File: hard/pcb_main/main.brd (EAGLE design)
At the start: 230 x 150 mm, 865 parts

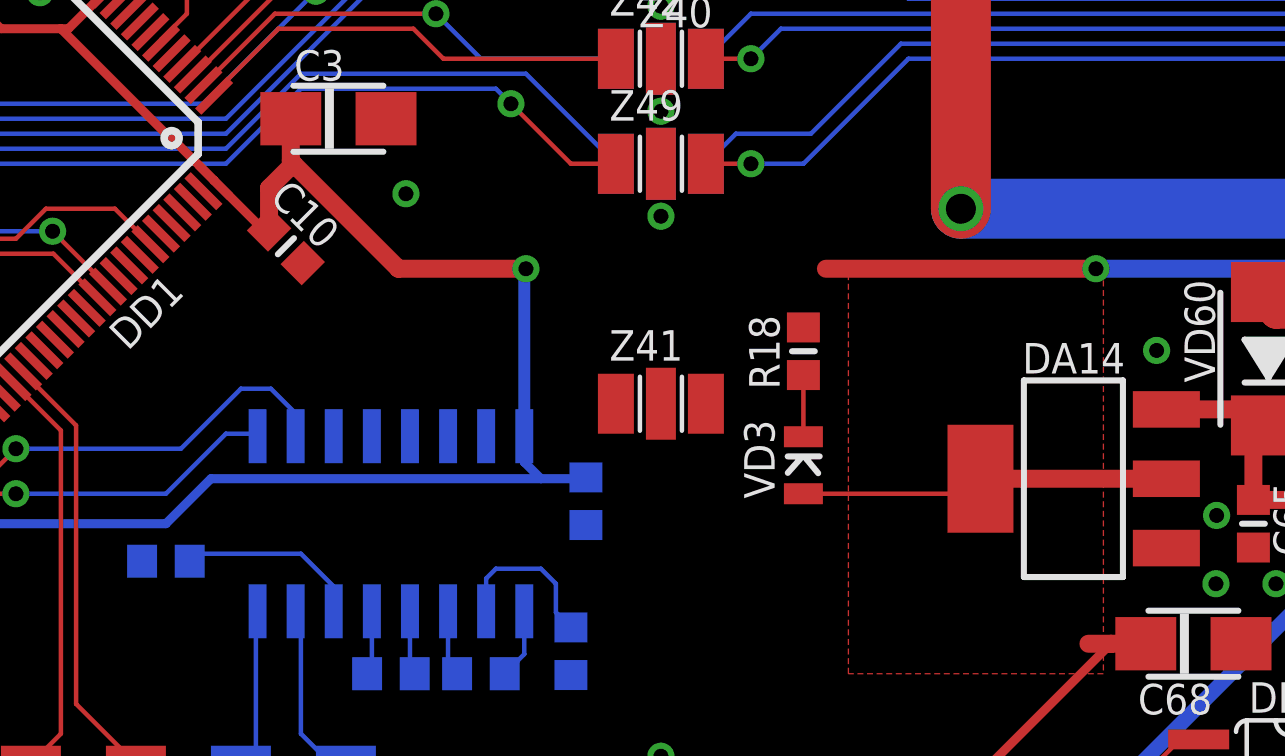
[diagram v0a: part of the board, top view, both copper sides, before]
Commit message: filters addition completed
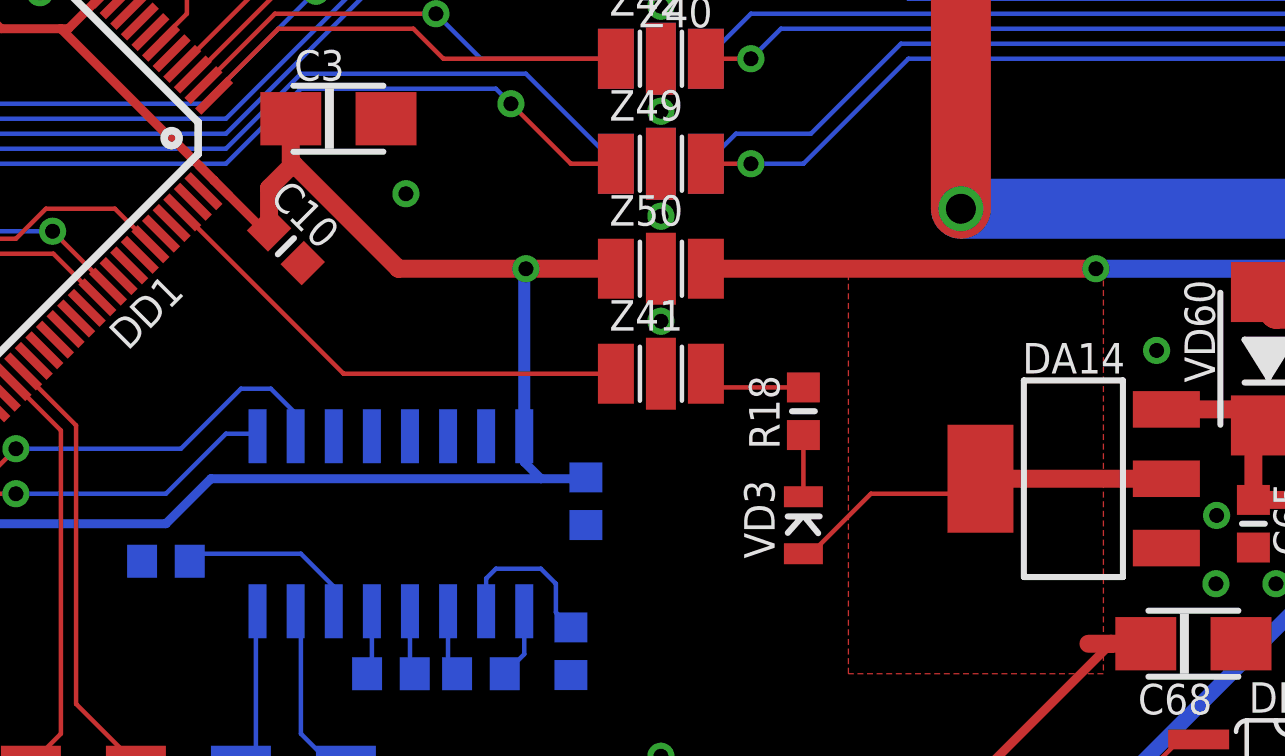
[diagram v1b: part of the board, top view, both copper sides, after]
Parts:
- added Z50: NFE31PT, emi-filter:NFE31
- moved R18 2.00 mm to (72.2, 65.8)
- moved VD3 2.00 mm to (72.2, 62.0)
- moved Z41 1.00 mm to (67.5, 67.0)
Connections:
- new net +3V3_DIRT: C1.1, C10.1, C143.1, C2.1, C3.+, C7.1, C9.1, DA17.16, DD1.100, DD1.11, DD1.28, DD1.50, DD1.6, DD1.75, L1.1, Z50.1
- net +3V3: now also Z50.3; no longer C1.1, C10.1, C143.1, C2.1, C3.+, C7.1, C9.1, DA17.16, DD1.100, DD1.11, DD1.28, DD1.50, DD1.6, DD1.75, L1.1
- net GND: now also Z50.2
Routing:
- net +3V3_DIRT: track 0.00 -> 99.6 mm, vias 0 -> 3
- net +3V3: track 902.7 -> 810.8 mm, vias 20 -> 17
- net N$350: track 0.00 -> 16.7 mm
- net N$272: track 0.00 -> 3.44 mm
- net GND: vias 169 -> 170

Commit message: nop
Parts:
- moved C3 2.12 mm to (55.2, 74.0), turned to 315 degrees
- moved VD1 0.52 mm to (7.88, 100.8)
- moved Z10 0.50 mm to (15.0, 74.0)
- moved Z11 0.50 mm to (15.0, 81.0)
- moved Z12 0.50 mm to (15.0, 77.5)
- moved Z13 0.50 mm to (57.0, 53.0)
- moved Z14 0.50 mm to (53.5, 53.0)
- moved Z15 0.50 mm to (46.5, 53.0)
- moved Z16 0.50 mm to (50.0, 53.0)
- moved Z17 0.50 mm to (32.5, 53.0)
- moved Z18 0.50 mm to (36.0, 53.0)
- moved Z19 0.50 mm to (22.0, 53.0)
- moved Z3 0.50 mm to (15.0, 60.0)
- moved Z34 0.50 mm to (15.0, 88.0)
- moved Z35 0.50 mm to (15.0, 91.5)
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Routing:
- net GND: track 33.8 -> 411.8 mm, vias 170 -> 191
- net +3V3_DIRT: track 99.6 -> 96.7 mm
- net N$314: track 22.9 -> 24.2 mm
- net N$355: track 14.4 -> 13.5 mm
- net N$237: track 6.07 -> 5.28 mm
- net N$334: track 37.2 -> 37.8 mm
- net +24V_CLEAR: track 466.8 -> 466.2 mm
- net N$343: track 11.9 -> 12.5 mm
- net D-: track 57.0 -> 57.5 mm
- net N$346: track 8.08 -> 7.58 mm
- net USB_PRESENT: track 34.7 -> 34.2 mm
- net USB_DISCOVERY: track 33.0 -> 32.5 mm
- net TO_RS232: track 35.9 -> 36.4 mm
- net TACHOMETER: track 18.6 -> 18.1 mm
- net N$356: track 66.0 -> 66.5 mm
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
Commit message: nop
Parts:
- removed R365: 10kOhm, rcl:R0603
- removed R366: 47kOhm, rcl:R0603
- removed R367, R368: 1kOhm, rcl:R0805
- added R17, R21: 100Ohm, rcl:R0603
- added R25: 1kOhm, rcl:R0805
- added R28: 1kOhm, rcl:R2512
- C3: value 10uF/10V -> 22pF; device rcl:A/3216-18W -> rcl:C0603
- C49: value 0.1uF -> 5600pF
- C5: value 22pF -> 10uF/10V; device rcl:C0603 -> rcl:A/3216-18W
- C50: value 5600pF -> 0.1uF
- C7: value 0.1uF -> 1uF/16V
- C8: value 1uF/16V -> 0.1uF
- R10: value 10kOhm -> 0Ohm; device rcl:R0603 -> rcl:R0805
- R100, R90, R95: value 2.2kOhm/5% -> 10kOhm
- R101, R102, R103, R104, R74, R75, R76: value 10kOhm -> 1.2kOhm/5%
- R107, R108, R109, R110: value 1.2kOhm/5% -> 22kOhm/5%
- R113, R114, R115: value 22kOhm/5% -> 1.2kOhm/5%
- R116: value 22kOhm/5% -> 1kOhm; device rcl:R0603 -> rcl:RTRIMTSM53YJ
- R117, R118, R119: value 1.2kOhm/5% -> 51kOhm/5%
- R120: value 1kOhm -> 51kOhm/5%; device rcl:RTRIMTSM53YJ -> rcl:R0603
- R124, R125: value 51kOhm/5% -> 1kOhm; device rcl:R0603 -> rcl:R2512
- R126, R127: value 51kOhm/5% -> 100kOhm
- R128, R129: value 1kOhm -> 36kOhm; device rcl:R2512 -> rcl:R0603
- R131: value 100kOhm -> 15kOhm; device rcl:R0603 -> rcl:R0805
- R132: value 36kOhm -> 82kOhm; device rcl:R0603 -> rcl:R0805
- R133: value 36kOhm -> 470kOhm; device rcl:R0603 -> rcl:R0805
- R134: value 100kOhm -> 1kOhm; device rcl:R0603 -> rcl:R0805
- R135: value 15kOhm -> 3.3kOhm; device rcl:R0805 -> rcl:R2512
- R136: value 82kOhm -> 330Ohm; device rcl:R0805 -> rcl:R0603
- R137: value 470kOhm -> 330Ohm; device rcl:R0805 -> rcl:R0603
- R138, R190, R191: value 1kOhm -> 4.7kOhm; device rcl:R0805 -> rcl:R1206
- R139: value 3.3kOhm -> 4.7kOhm; device rcl:R2512 -> rcl:R1206
- R140, R141: value 330Ohm -> 4.7kOhm; device rcl:R0603 -> rcl:R1206
- R15, R342, R343, R344, R345: value 100Ohm -> 1kOhm; device rcl:R0603 -> rcl:R0805
- R154, R155, R156, R157, R205, R206, R207, R208, R253, R254, R255, R256, R301, R302, R303, R304: value 4.7kOhm -> 1kOhm; device rcl:R1206 -> rcl:R2512
- R170, R171, R172, R173, R221, R222, R223, R224, R269, R270, R271, R272, R317, R318, R319, R320: value 1kOhm -> 10kOhm; device rcl:R2512 -> rcl:R0603
- R18: value 330Ohm -> 100Ohm
- R186, R187, R363: value 10kOhm -> 1kOhm; device rcl:R0603 -> rcl:R0805
- R189, R192, R237, R238, R239, R240, R285, R286, R287, R288: value 10kOhm -> 4.7kOhm; device rcl:R0603 -> rcl:R1206
- R20: value 100Ohm -> 330Ohm
- R22: value 1kOhm -> 100Ohm; device rcl:R0805 -> rcl:R0603
- R26, R27: value 100Ohm -> 1kOhm; device rcl:R0603 -> rcl:R2512
- R29: device rcl:R0805 -> rcl:R2512
- R334, R335, R336, R337: value 10kOhm -> 100Ohm
- R34, R35, R36, R37, R58, R59, R60, R61: value 1kOhm -> 100kOhm; device rcl:R2512 -> rcl:R0603
- R358: value 1kOhm -> 120Ohm; device rcl:R0805 -> rcl:R1206
- R359, R361: value 1kOhm -> 10kOhm; device rcl:R0805 -> rcl:R0603
- R360: value 1kOhm -> 36kOhm; device rcl:R0805 -> rcl:R0603
- R362: value 120Ohm -> 47kOhm; device rcl:R1206 -> rcl:R0603
- R364: value 36kOhm -> 1kOhm; device rcl:R0603 -> rcl:R0805
- R42, R43, R44, R45, R66, R67, R68, R69, R87, R88, R89: value 100kOhm -> 10kOhm
- R50, R51, R52, R53: value 10kOhm -> 1kOhm; device rcl:R0603 -> rcl:R2512
- R77: value 10kOhm -> 5.1kOhm/1%
- R78, R79, R80: value 1.2kOhm/5% -> 5.1kOhm/1%
- R8: value 0Ohm -> 10kOhm; device rcl:R0805 -> rcl:R0603
- R83, R84, R85: value 5.1kOhm/1% -> 100kOhm
- R86: value 5.1kOhm/1% -> 2.2kOhm/5%
- R91, R96: value 10kOhm -> 2.2kOhm/5%
- VD212: value 3.3V -> SMBJ24CA; device diode:SOD80 -> diode:SMB-BIDIR
- VD214: value SMBJ24CA -> 3.3V; device diode:SMB-BIDIR -> diode:SOD80
- Z1: value 4701-001LF -> NFE31PT; device emi-filter:TUSONIX-4701 -> emi-filter:NFE31
- Z41: value NFE31PT -> 4701-001LF; device emi-filter:NFE31 -> emi-filter:TUSONIX-4701
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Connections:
- net !SR_OUT_ENABLE: now also R21.1, R333.1; no longer R19.1, R337.1
- net !SR_SAMPLE: now also R23.1; no longer R20.1
- net +24V_CLEAR: now also R26.1, R27.1, R28.1, R29.1, R50.1, R51.1, R52.1, R53.1, Z41.3; no longer R34.1, R35.1, R36.1, R37.1, R58.1, R59.1, R60.1, R61.1, Z1.3
- net +3V3: now also C142.2, R15.1, R170.1, R171.1, R172.1, R173.1, R221.1, R222.1, R223.1, R224.1, R25.1, R269.1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; no longer C145.2, R10.2, R186.1, R187.1, R188.1, R189.1, R22.1, R237.1, R238.1, R239.1, R240.1, R285.1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
- net +3V3_DIRT: now also C144.1, C5.+, C6.1, C8.1, Z1.1; no longer C10.1, C143.1, C3.+, C7.1, Z50.1
- net +5V: now also C50.1, R113.1, R114.1, R115.1, R116.1, R117.2, R118.2, R119.2, R120.2, R136.1; no longer C49.1, R117.1, R118.1, R119.1, R120.1, R124.2, R125.2, R126.2, R127.2, R140.1
- net +5V_USB: now also R359.2, R361.2; no longer R363.2, R365.2
- net -5V: now also R116.3, R137.2; no longer R120.3, R141.2
- net AGND: now also R42.1, R43.1, R44.1, R45.1, R66.1, R67.1, R68.1, R69.1, Z5.1; no longer R50.1, R51.1, R52.1, R53.1, R74.1, R75.1, R76.1, R77.1, Z2.1
- net AN_FILTERED_0: now also Z22.3; no longer Z20.3
- net AN_FILTERED_1: now also Z23.3; no longer Z21.3
- net AN_FILTERED_10: now also Z32.3; no longer Z30.3
- net AN_FILTERED_11: now also Z33.3; no longer Z31.3
- net AN_FILTERED_12: now also Z34.3; no longer Z32.3
- net AN_FILTERED_13: now also Z35.3; no longer Z33.3
- net AN_FILTERED_14: now also Z36.3; no longer Z34.3
- net AN_FILTERED_15: now also Z37.3; no longer Z35.3
- net AN_FILTERED_2: now also Z24.3; no longer Z22.3
- net AN_FILTERED_3: now also Z25.3; no longer Z23.3
- net AN_FILTERED_4: now also Z26.3; no longer Z24.3
- net AN_FILTERED_5: now also Z27.3; no longer Z25.3
- net AN_FILTERED_6: now also Z28.3; no longer Z26.3
- net AN_FILTERED_7: now also Z29.3; no longer Z27.3
- net AN_FILTERED_8: now also Z30.3; no longer Z28.3
- net AN_FILTERED_9: now also Z31.3; no longer Z29.3
- net AN_RAW_0: now also R26.2; no longer R30.2
- net AN_RAW_1: now also R27.2; no longer R31.2
- net AN_RAW_10: now also R52.2; no longer R56.2
- net AN_RAW_11: now also R53.2; no longer R57.2
- net AN_RAW_12: now also R54.2; no longer R58.2
- net AN_RAW_13: now also R55.2; no longer R59.2
- net AN_RAW_14: now also R56.2; no longer R60.2
- net AN_RAW_15: now also R57.2; no longer R61.2
- net AN_RAW_2: now also R28.2; no longer R32.2
- net AN_RAW_3: now also R29.2; no longer R33.2
- net AN_RAW_4: now also R30.2; no longer R34.2
- net AN_RAW_5: now also R31.2; no longer R35.2
- net AN_RAW_6: now also R32.2; no longer R36.2
- net AN_RAW_7: now also R33.2; no longer R37.2
- net AN_RAW_8: now also R50.2; no longer R54.2
- net AN_RAW_9: now also R51.2; no longer R55.2
- net BOOT_0: now also Z10.3; no longer Z6.3
- net BOOT_1: now also Z9.3; no longer Z5.3
- net CANL: now also R358.2; no longer R362.2
- net CAN_RX: now also Z47.3; no longer Z15.3
- net CAN_TX: now also Z50.3; no longer Z16.3
- net D+: now also Z42.3; no longer Z18.3
- net D-: now also Z43.3; no longer Z17.3
- net DISCRETE_1: now also R170.2; no longer R174.2
- net DISCRETE_10: now also R179.2; no longer R183.2
- net DISCRETE_11: now also R180.2; no longer R184.2
- net DISCRETE_12: now also R181.2; no longer R185.2
- net DISCRETE_13: now also R182.2; no longer R186.2
- net DISCRETE_14: now also R183.2; no longer R187.2
- net DISCRETE_15: now also R184.2; no longer R188.2
- net DISCRETE_16: now also R185.2; no longer R189.2
- net DISCRETE_17: now also R221.2; no longer R225.2
- net DISCRETE_18: now also R222.2; no longer R226.2
- net DISCRETE_19: now also R223.2; no longer R227.2
- net DISCRETE_2: now also R171.2; no longer R175.2
- net DISCRETE_20: now also R224.2; no longer R228.2
- net DISCRETE_21: now also R225.2; no longer R229.2
- net DISCRETE_22: now also R226.2; no longer R230.2
- net DISCRETE_23: now also R227.2; no longer R231.2
- net DISCRETE_24: now also R228.2; no longer R232.2
- net DISCRETE_25: now also R229.2; no longer R233.2
- net DISCRETE_26: now also R230.2; no longer R234.2
- net DISCRETE_27: now also R231.2; no longer R235.2
- net DISCRETE_28: now also R232.2; no longer R236.2
- net DISCRETE_29: now also R233.2; no longer R237.2
- net DISCRETE_3: now also R172.2; no longer R176.2
- net DISCRETE_30: now also R234.2; no longer R238.2
- net DISCRETE_31: now also R235.2; no longer R239.2
- net DISCRETE_32: now also R236.2; no longer R240.2
- net DISCRETE_33: now also R269.2; no longer R273.2
- net DISCRETE_34: now also R270.2; no longer R274.2
- net DISCRETE_35: now also R271.2; no longer R275.2
- net DISCRETE_36: now also R272.2; no longer R276.2
- net DISCRETE_37: now also R273.2; no longer R277.2
- net DISCRETE_38: now also R274.2; no longer R278.2
- net DISCRETE_39: now also R275.2; no longer R279.2
- net DISCRETE_4: now also R173.2; no longer R177.2
- net DISCRETE_40: now also R276.2; no longer R280.2
- net DISCRETE_41: now also R277.2; no longer R281.2
- net DISCRETE_42: now also R278.2; no longer R282.2
- net DISCRETE_43: now also R279.2; no longer R283.2
- net DISCRETE_44: now also R280.2; no longer R284.2
- net DISCRETE_45: now also R281.2; no longer R285.2
- net DISCRETE_46: now also R282.2; no longer R286.2
- net DISCRETE_47: now also R283.2; no longer R287.2
- net DISCRETE_48: now also R284.2; no longer R288.2
- net DISCRETE_49: now also R317.2; no longer R321.2
- net DISCRETE_5: now also R174.2; no longer R178.2
- net DISCRETE_50: now also R318.2; no longer R322.2
- net DISCRETE_51: now also R319.2; no longer R323.2
- net DISCRETE_52: now also R320.2; no longer R324.2
- net DISCRETE_53: now also R321.2; no longer R325.2
- net DISCRETE_54: now also R322.2; no longer R326.2
- net DISCRETE_55: now also R323.2; no longer R327.2
- net DISCRETE_56: now also R324.2; no longer R328.2
- net DISCRETE_57: now also R325.2; no longer R329.2
- net DISCRETE_58: now also R326.2; no longer R330.2
- net DISCRETE_59: now also R327.2; no longer R331.2
- net DISCRETE_6: now also R175.2; no longer R179.2
- net DISCRETE_60: now also R328.2; no longer R332.2
- net DISCRETE_61: now also R329.2; no longer R333.2
- net DISCRETE_62: now also R330.2; no longer R334.2
- net DISCRETE_63: now also R331.2; no longer R335.2
- net DISCRETE_64: now also R332.2; no longer R336.2
- net DISCRETE_7: now also R176.2; no longer R180.2
- net DISCRETE_8: now also R177.2; no longer R181.2
- net DISCRETE_9: now also R178.2; no longer R182.2
- net FREQ_RAW: now also R125.2; no longer R129.2
- net FROM_RS232: now also VD213.A2, Z46.1; no longer VD214.A2, Z14.1
- net GND: now also C142.1, C145.2, C3.2, C5.-, C8.2, R10.1, R100.1, R104.2, R105.2, R106.2, R128.1, R129.1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; no longer C142.2, C145.1, C3.-, C5.2, C7.2, R100.2, R104.1, R108.2, R109.2, R110.2, R132.1, R137.1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
- net I2C_SDA: now also R15.2, Z17.1; no longer R22.2, Z12.1
- net JTDI: now also Z6.1; no longer Z4.1
- net JTDO: now also Z4.1; no longer Z9.1
- net JTMS: now also Z3.1; no longer Z8.1
- net JTRST: now also Z2.1; no longer Z3.1
- net N$1: now also R357.2; no longer R361.2
- net N$10: now also R350.2; no longer R354.2
- net N$100: now also R244.2; no longer R248.2
- net N$101: now also R245.2; no longer R249.2
- net N$102: now also R246.2; no longer R250.2
- net N$103: now also R247.2; no longer R251.2
- net N$104: now also R248.2; no longer R252.2
- net N$105: now also R249.2; no longer R253.2
- net N$106: now also R250.2; no longer R254.2
- net N$107: now also R251.2; no longer R255.2
- net N$108: now also R252.2; no longer R256.2
- net N$109: now also R254.2; no longer R258.2
- net N$11: now also R341.1; no longer R345.1
- net N$110: now also R301.2; no longer R305.2
- net N$111: now also R255.2; no longer R259.2
- net N$112: now also R302.2; no longer R306.2
- net N$113: now also R256.2; no longer R260.2
- net N$114: now also R303.2; no longer R307.2
- net N$115: now also R257.2; no longer R261.2
- net N$116: now also R304.2; no longer R308.2
- net N$117: now also R258.2; no longer R262.2
- net N$118: now also R305.2; no longer R309.2
- net N$119: now also R259.2; no longer R263.2
- net N$120: now also R306.2; no longer R310.2
- net N$121: now also R260.2; no longer R264.2
- net N$122: now also R307.2; no longer R311.2
- net N$123: now also R261.2; no longer R265.2
- net N$124: now also R308.2; no longer R312.2
- net N$125: now also R262.2; no longer R266.2
- net N$126: now also R309.2; no longer R313.2
- net N$127: now also R263.2; no longer R267.2
- net N$128: now also R310.2; no longer R314.2
- net N$129: now also R264.2; no longer R268.2
- net N$130: now also R311.2; no longer R315.2
- net N$131: now also R265.2; no longer R269.2
- net N$132: now also R312.2; no longer R316.2
- net N$133: now also R266.2; no longer R270.2
- net N$134: now also R313.2; no longer R317.2
- net N$135: now also R267.2; no longer R271.2
- net N$136: now also R314.2; no longer R318.2
- net N$137: now also R268.2; no longer R272.2
- net N$138: now also R315.2; no longer R319.2
- net N$139: now also R316.2; no longer R320.2
- net N$14: now also C4.1; no longer C5.1
- net N$140: now also R285.2; no longer R289.2
- net N$141: now also R286.2; no longer R290.2
- net N$142: now also R287.2; no longer R291.2
- net N$143: now also R288.2; no longer R292.2
- net N$144: now also R289.2; no longer R293.2
- net N$145: now also R290.2; no longer R294.2
- net N$146: now also R291.2; no longer R295.2
- net N$147: now also R292.2; no longer R296.2
- net N$148: now also R293.2; no longer R297.2
- net N$149: now also R294.2; no longer R298.2
- net N$15: now also C3.1; no longer C4.1
- net N$150: now also R295.2; no longer R299.2
- net N$151: now also R296.2; no longer R300.2
- net N$152: now also R297.2; no longer R301.2
- net N$153: now also R298.2; no longer R302.2
- net N$154: now also R299.2; no longer R303.2
- net N$155: now also R300.2; no longer R304.2
- net N$156: now also R205.2; no longer R209.2
- net N$157: now also R206.2; no longer R210.2
- net N$158: now also R207.2; no longer R211.2
- net N$159: now also R208.2; no longer R212.2
- net N$16: now also Z12.1; no longer Z46.1
- net N$160: now also R209.2; no longer R213.2
- net N$161: now also R210.2; no longer R214.2
- net N$162: now also R211.2; no longer R215.2
- net N$163: now also R212.2; no longer R216.2
- net N$164: now also R213.2; no longer R217.2
- net N$165: now also R214.2; no longer R218.2
- net N$166: now also R215.2; no longer R219.2
- net N$167: now also R216.2; no longer R220.2
- net N$168: now also R217.2; no longer R221.2
- net N$169: now also R218.2; no longer R222.2
- net N$170: now also R219.2; no longer R223.2
- net N$171: now also R220.2; no longer R224.2
- net N$172: now also R189.2; no longer R193.2
- net N$173: now also R190.2; no longer R194.2
- net N$174: now also R191.2; no longer R195.2
- net N$175: now also R192.2; no longer R196.2
- net N$176: now also R193.2; no longer R197.2
- net N$177: now also R194.2; no longer R198.2
- net N$178: now also R195.2; no longer R199.2
- net N$179: now also R196.2; no longer R200.2
- net N$180: now also R197.2; no longer R201.2
- net N$181: now also R198.2; no longer R202.2
- net N$182: now also R199.2; no longer R203.2
- net N$183: now also R200.2; no longer R204.2
- net N$184: now also R201.2; no longer R205.2
- net N$185: now also R202.2; no longer R206.2
- net N$186: now also R203.2; no longer R207.2
- net N$187: now also R204.2; no longer R208.2
- net N$188: now also R154.2; no longer R158.2
- net N$189: now also R155.2; no longer R159.2
- net N$190: now also R156.2; no longer R160.2
- net N$191: now also R157.2; no longer R161.2
- net N$192: now also R158.2; no longer R162.2
- net N$193: now also R159.2; no longer R163.2
- net N$194: now also R160.2; no longer R164.2
- net N$195: now also R161.2; no longer R165.2
- net N$196: now also R162.2; no longer R166.2
- net N$197: now also R163.2; no longer R167.2
- net N$198: now also R164.2; no longer R168.2
- net N$199: now also R165.2; no longer R169.2
- net N$200: now also R166.2; no longer R170.2
- net N$201: now also R167.2; no longer R171.2
- net N$202: now also R168.2; no longer R172.2
- net N$203: now also R169.2; no longer R173.2
- net N$204: now also R138.2; no longer R142.2
- net N$205: now also R139.2; no longer R143.2
- net N$206: now also R140.2; no longer R144.2
- net N$207: now also R141.2; no longer R145.2
- net N$208: now also R142.2; no longer R146.2
- net N$209: now also R143.2; no longer R147.2
- net N$21: now also R135.1; no longer R139.1
- net N$210: now also R144.2; no longer R148.2
- net N$211: now also R145.2; no longer R149.2
- net N$212: now also R146.2; no longer R150.2
- net N$213: now also R147.2; no longer R151.2
- net N$214: now also R148.2; no longer R152.2
- net N$215: now also R149.2; no longer R153.2
- net N$216: now also R150.2; no longer R154.2
- net N$217: now also R151.2; no longer R155.2
- net N$218: now also R152.2; no longer R156.2
- net N$219: now also R153.2; no longer R157.2
- net N$220: now also Z18.1; no longer Z47.1
- net N$221: now also Z13.1; no longer Z49.1
- net N$222: now also Z19.1; no longer Z48.1
- net N$223: now also Z20.1; no longer Z42.1
- net N$224: now also R358.1; no longer R362.1
- net N$226: now also C7.1; no longer C8.1
- net N$227: now also R362.1, R364.1; no longer R366.1, R368.1
- net N$228: now also R359.1, R360.2; no longer R363.1, R364.2
- net N$229: now also Z44.3; no longer Z37.3
- net N$230: now also R361.1, R363.1, VD214.C; no longer R365.1, R367.1, VD212.C
- net N$233: now also C143.1; no longer C142.1
- net N$235: now also C145.1; no longer C144.1
- net N$236: now also Z46.3; no longer Z14.3
- net N$237: now also Z45.3; no longer Z13.3
- net N$24: now also R132.2; no longer R136.2
- net N$242: now also Z50.1; no longer Z16.1
- net N$243: now also R124.1, R126.1; no longer R128.1, R130.1
- net N$244: now also R134.2, Z41.1; no longer R138.2, Z1.1
- net N$248: now also R130.1; no longer R134.1
- net N$249: now also R104.1, R107.1; no longer R111.1, R112.1
- net N$25: now also R131.2; no longer R135.2
- net N$250: now also R107.2, R113.2; no longer R111.2, R117.2
- net N$252: now also R80.2; no longer R84.2
- net N$253: now also R117.1; no longer R121.1
- net N$254: now also R81.2; no longer R85.2
- net N$256: now also R77.2; no longer R81.2
- net N$259: now also R101.2; no longer R105.2
- net N$26: now also R131.1, R132.1, R135.2; no longer R135.1, R136.1, R139.2
- net N$260: now also R118.1; no longer R122.1
- net N$261: now also C49.1, R123.1; no longer C50.1, R127.1
- net N$262: now also R83.2; no longer R87.2
- net N$266: now also R136.2; no longer R140.2
- net N$267: now also R137.1; no longer R141.1
- net N$268: now also R20.2; no longer R18.2
- net N$269: now also R88.1, R89.2; no longer R92.1, R93.2
- net N$27: now also R134.1; no longer R138.1
- net N$270: now also R83.1, R89.1, R90.2; no longer R87.1, R93.1, R94.2
- net N$271: now also R87.1, R88.2; no longer R91.1, R92.2
- net N$272: now also R20.1, Z14.3; no longer R18.1, Z41.3
- net N$273: now also R188.2; no longer R192.2
- net N$274: now also R101.1, R86.1, R87.2; no longer R105.1, R90.1, R91.2
- net N$275: now also Z15.1; no longer Z44.1
- net N$276: now also Z21.1; no longer Z43.1
- net N$277: now also Z16.1; no longer Z45.1
- net N$279: now also R78.2; no longer R82.2
- net N$28: now also R133.2; no longer R137.2
- net N$280: now also R84.2; no longer R88.2
- net N$281: now also R93.1, R94.2; no longer R97.1, R98.2
- net N$282: now also R84.1, R94.1, R95.2; no longer R88.1, R98.1, R99.2
- net N$283: now also R92.1, R93.2; no longer R96.1, R97.2
- net N$284: now also R102.1, R91.1, R92.2; no longer R106.1, R95.1, R96.2
- net N$285: now also R102.2; no longer R106.2
- net N$286: now also R105.1, R110.1; no longer R113.1, R114.1
- net N$287: now also R109.2, R114.2; no longer R113.2, R118.2
- net N$288: now also R119.1; no longer R123.1
- net N$290: now also R120.1; no longer R124.1
- net N$295: now also R82.2; no longer R86.2
- net N$297: now also R79.2; no longer R83.2
- net N$298: now also R85.2; no longer R89.2
- net N$299: now also R98.1, R99.2; no longer R102.1, R103.2
- net N$3: now also R356.2; no longer R360.2
- net N$30: now also R34.1; no longer R38.1
- net N$300: now also R100.2, R85.1, R99.1; no longer R103.1, R104.2, R89.1
- net N$301: now also R97.1, R98.2; no longer R101.1, R102.2
- net N$302: now also R103.1, R96.1, R97.2; no longer R100.1, R101.2, R107.1
- net N$303: now also R103.2; no longer R107.2
- net N$304: now also R106.1, R111.1, R112.1; no longer R110.1, R115.1, R116.1
- net N$305: now also R111.2; no longer R119.2
- net N$306: now also R121.1; no longer R125.1
- net N$308: now also R122.1; no longer R126.1
- net N$31: now also R35.1; no longer R39.1
- net N$312: now also R108.2, R110.2; no longer R114.2, R120.2
- net N$313: now also R125.1, R127.1; no longer R129.1, R131.1
- net N$314: now also Z47.1; no longer Z15.1
- net N$315: now also R34.2, R42.2, Z22.1; no longer R38.2, R46.2, Z20.1
- net N$316: now also R35.2, R43.2, Z23.1; no longer R39.2, R47.2, Z21.1
- net N$317: now also R36.2, R44.2, Z24.1; no longer R40.2, R48.2, Z22.1
- net N$318: now also R37.2, R45.2, Z25.1; no longer R41.2, R49.2, Z23.1
- net N$319: now also R38.2, R46.2, Z26.1; no longer R42.2, R50.2, Z24.1
- net N$32: now also R41.1; no longer R45.1
- net N$320: now also R39.2, R47.2, Z27.1; no longer R43.2, R51.2, Z25.1
- net N$321: now also R40.2, R48.2, Z28.1; no longer R44.2, R52.2, Z26.1
- net N$322: now also R41.2, R49.2, Z29.1; no longer R45.2, R53.2, Z27.1
- net N$323: now also R58.2, R66.2, Z30.1; no longer R62.2, R70.2, Z28.1
- net N$324: now also R59.2, R67.2, Z31.1; no longer R63.2, R71.2, Z29.1
- net N$325: now also R60.2, R68.2, Z32.1; no longer R64.2, R72.2, Z30.1
- net N$326: now also R61.2, R69.2, Z33.1; no longer R65.2, R73.2, Z31.1
- net N$327: now also R62.2, R70.2, Z34.1; no longer R66.2, R74.2, Z32.1
- net N$328: now also R63.2, R71.2, Z35.1; no longer R67.2, R75.2, Z33.1
- net N$329: now also R64.2, R72.2, Z36.1; no longer R68.2, R76.2, Z34.1
- net N$33: now also R40.1; no longer R44.1
- net N$330: now also R65.2, R73.2, Z37.1; no longer R69.2, R77.2, Z35.1
- net N$331: now also C7.2, R10.2, Z5.3; no longer C8.2, R8.2, Z2.3
- net N$332: now also Z10.1; no longer Z6.1
- net N$333: now also Z9.1; no longer Z5.1
- net N$334: now also Z2.3; no longer Z3.3
- net N$335: now also Z6.3; no longer Z4.3
- net N$336: now also Z3.3; no longer Z8.3
- net N$337: now also C10.1, R9.1, Z8.3; no longer C6.1, R10.1, Z10.3
- net N$339: now also R8.1, Z4.3; no longer R9.1, Z9.3
- net N$34: now also R39.1; no longer R43.1
- net N$340: now also Z17.3; no longer Z12.3
- net N$341: now also R25.2; no longer R29.2
- net N$342: now also Z44.1; no longer Z37.1
- net N$343: now also R364.2, Z49.1; no longer R368.2, Z36.1
- net N$344: now also R363.2, Z48.1; no longer R367.2, Z19.1
- net N$345: now also Z43.1; no longer Z17.1
- net N$346: now also Z42.1; no longer Z18.1
- net N$347: now also R126.2, R128.2, VD51.C; no longer R130.2, R132.2, VD50.C
- net N$348: now also R127.2, R129.2, VD52.C; no longer R131.2, R133.2, VD51.C
- net N$349: now also R130.2, VD50.C; no longer R134.2, VD52.C
- net N$35: now also R38.1; no longer R42.1
- net N$350: now also Z14.1; no longer Z41.1
- net N$351: now also R21.2, Z20.3; no longer R19.2, Z42.3
- net N$352: now also R22.2, Z15.3; no longer R26.2, Z44.3
- net N$353: now also R23.2, Z21.3; no longer R20.2, Z43.3
- net N$354: now also R24.2, Z16.3; no longer R27.2, Z45.3
- net N$355: now also R16.2, Z12.3; no longer R15.2, Z46.3
- net N$356: now also R18.2, Z13.3; no longer R16.2, Z49.3
- net N$357: now also R17.2, Z18.3; no longer R23.2, Z47.3
- net N$358: now also R19.2, Z19.3; no longer R24.2, Z48.3
- net N$36: now also R37.1; no longer R41.1
- net N$37: now also R36.1; no longer R40.1
- net N$38: now also R58.1; no longer R62.1
- net N$39: now also R60.1; no longer R64.1
- net N$4: now also R355.2; no longer R359.2
- net N$40: now also R59.1; no longer R63.1
- net N$41: now also R61.1; no longer R65.1
- net N$42: now also R62.1; no longer R66.1
- net N$43: now also R64.1; no longer R68.1
- net N$44: now also R63.1; no longer R67.1
- net N$45: now also R65.1; no longer R69.1
- net N$46: now also R350.1; no longer R354.1
- net N$47: now also R351.1; no longer R355.1
- net N$48: now also R352.1; no longer R356.1
- net N$49: now also R353.1; no longer R357.1
- net N$5: now also R354.2; no longer R358.2
- net N$50: now also R354.1; no longer R358.1
- net N$51: now also R355.1; no longer R359.1
- net N$52: now also R356.1; no longer R360.1
- net N$53: now also R357.1; no longer R361.1
- net N$54: now also R340.1; no longer R344.1
- net N$55: now also R339.1; no longer R343.1
- net N$56: now also R338.1; no longer R342.1
- net N$57: now also R337.1; no longer R341.1
- net N$58: now also R336.1; no longer R340.1
- net N$59: now also R335.1; no longer R339.1
- net N$6: now also R353.2; no longer R357.2
- net N$60: now also R334.1; no longer R338.1
- net N$61: now also R334.2; no longer R338.2
- net N$70: now also R335.2; no longer R339.2
- net N$71: now also R336.2; no longer R340.2
- net N$72: now also R341.2; no longer R345.2
- net N$73: now also R340.2; no longer R344.2
- net N$74: now also R339.2; no longer R343.2
- net N$75: now also R342.2; no longer R346.2
- net N$76: now also R343.2; no longer R347.2
- net N$77: now also R344.2; no longer R348.2
- net N$78: now also R345.2; no longer R349.2
- net N$79: now also R346.2; no longer R350.2
- net N$8: now also R352.2; no longer R356.2
- net N$80: now also R337.2; no longer R341.2
- net N$81: now also R338.2; no longer R342.2
- net N$82: now also R347.2; no longer R351.2
- net N$83: now also R348.2; no longer R352.2
- net N$84: now also R349.2; no longer R353.2
- net N$88: now also R186.2; no longer R190.2
- net N$89: now also R186.1; no longer R190.1
- net N$9: now also R351.2; no longer R355.2
- net N$91: now also R237.2; no longer R241.2
- net N$92: now also R187.2; no longer R191.2
- net N$93: now also R238.2; no longer R242.2
- net N$94: now also R239.2; no longer R243.2
- net N$95: now also R240.2; no longer R244.2
- net N$96: now also R253.2; no longer R257.2
- net N$97: now also R241.2; no longer R245.2
- net N$98: now also R242.2; no longer R246.2
- net N$99: now also R243.2; no longer R247.2
- net PHASE_1: now also R74.2, R77.1, R80.1; no longer R78.2, R81.1, R84.1
- net PHASE_2: now also R75.2, R78.1, R81.1; no longer R79.2, R82.1, R85.1
- net PHASE_3: now also R76.2, R79.1, R82.1; no longer R80.2, R83.1, R86.1
- net RAW_DISCRETE_1: now also R138.1, R154.1; no longer R142.1, R158.1
- net RAW_DISCRETE_10: now also R147.1, R163.1; no longer R151.1, R167.1
- net RAW_DISCRETE_11: now also R148.1, R164.1; no longer R152.1, R168.1
- net RAW_DISCRETE_12: now also R149.1, R165.1; no longer R153.1, R169.1
- net RAW_DISCRETE_13: now also R150.1, R166.1; no longer R154.1, R170.1
- net RAW_DISCRETE_14: now also R151.1, R167.1; no longer R155.1, R171.1
- net RAW_DISCRETE_15: now also R152.1, R168.1; no longer R156.1, R172.1
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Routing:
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
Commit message: nop
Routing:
- net GND: vias 192 -> 177
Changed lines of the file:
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@@
 <contactref element="R129" pad="1"/>
 <contactref element="VD52" pad="A"/>
-<via x="48.5" y="66.75" extent="1-16" drill="0.5"/>
 <via x="44.5" y="69.25" extent="1-16" drill="0.5"/>
 <via x="39.25" y="76.25" extent="1-16" drill="0.5"/>
@@
 <via x="57.5" y="102" extent="1-16" drill="0.5"/>
 <via x="63.5" y="102" extent="1-16" drill="0.5"/>
-<via x="31.5" y="58.25" extent="1-16" drill="0.5"/>
 <polygon width="0.3" layer="16" spacing="0.7" isolate="0.2" rank="6">
 <vertex x="1" y="149"/>
@@
 <wire x1="35.75" y1="62.5" x2="35.75" y2="62" width="0.15" layer="1"/>
 <wire x1="35.75" y1="62" x2="37" y2="60.75" width="0.15" layer="1"/>
-<via x="37" y="60.75" extent="1-16" drill="0.5"/>
 <via x="39.75" y="64.25" extent="1-16" drill="0.5"/>
 <wire x1="100.375" y1="42.7938" x2="99" y2="42.7938" width="0.3" layer="1"/>
@@
 <via x="170.5" y="24.25" extent="1-16" drill="0.5"/>
 <via x="183.5" y="24.25" extent="1-16" drill="0.5"/>
-<via x="41.5" y="87.5" extent="1-16" drill="0.5"/>
-<via x="40" y="87.5" extent="1-16" drill="0.5"/>
+<via x="37" y="88.25" extent="1-16" drill="0.5"/>
 <contactref element="DD12" pad="8"/>
 <contactref element="DD12" pad="8"/>
 <via x="64.5" y="72.5" extent="1-16" drill="0.5"/>
-<via x="35.25" y="81.25" extent="1-16" drill="0.5"/>
-<via x="52" y="70.5" extent="1-16" drill="0.5"/>
 <via x="86" y="60" extent="1-16" drill="0.5"/>
 <via x="79" y="48" extent="1-16" drill="0.5"/>
@@
 <via x="53.25" y="83.25" extent="1-16" drill="0.5"/>
 <via x="29" y="73" extent="1-16" drill="0.5"/>
-<via x="46.5" y="88.25" extent="1-16" drill="0.5"/>
+<via x="48" y="91" extent="1-16" drill="0.5"/>
 <via x="51.5" y="85" extent="1-16" drill="0.5"/>
 <via x="57.25" y="89" extent="1-16" drill="0.5"/>
 <via x="153" y="97" extent="1-16" drill="0.5"/>
-<via x="68.5" y="102" extent="1-16" drill="0.5"/>
 <via x="20.25" y="95" extent="1-16" drill="0.5"/>
 <via x="16.75" y="95" extent="1-16" drill="0.5"/>
@@
 <via x="15" y="61.75" extent="1-16" drill="0.5"/>
 <via x="15" y="58.25" extent="1-16" drill="0.5"/>
-<via x="34" y="65.75" extent="1-16" drill="0.5"/>
 <contactref element="Z17" pad="2"/>
 <contactref element="Z11" pad="2"/>
@@
 <wire x1="67.5" y1="95" x2="67.5" y2="53" width="1" layer="16"/>
 <wire x1="67.5" y1="53" x2="15" y2="53" width="1" layer="16"/>
-<via x="43.7" y="87.5" extent="1-16" drill="0.5"/>
-<via x="33" y="70.75" extent="1-16" drill="0.5"/>
-<via x="75.5" y="76.5" extent="1-16" drill="0.5"/>
-<via x="75.5" y="81" extent="1-16" drill="0.5"/>
-<via x="75.5" y="84" extent="1-16" drill="0.5"/>
-<via x="75.5" y="88" extent="1-16" drill="0.5"/>
 <via x="56" y="98" extent="1-16" drill="0.5"/>
 <via x="50" y="98" extent="1-16" drill="0.5"/>
@@
 <via x="56.5" y="75.5" extent="1-16" drill="0.5"/>
 <via x="65" y="60.25" extent="1-16" drill="0.5"/>
-<via x="49" y="58.75" extent="1-16" drill="0.5"/>
 <via x="46.25" y="77.25" extent="1-16" drill="0.5"/>
 <via x="49.75" y="73.25" extent="1-16" drill="0.5"/>
@@
 <via x="106.5" y="75" extent="1-16" drill="0.5"/>
 <via x="106" y="67.5" extent="1-16" drill="0.5"/>
-<via x="10.5" y="98.5" extent="1-16" drill="0.5"/>
+<via x="8.75" y="98.75" extent="1-16" drill="0.5"/>
 </signal>
 <signal name="AN_RAW_0">
@@
 </signal>
 </signals>
-<errors>
-</errors>
 </board>
 </drawing>

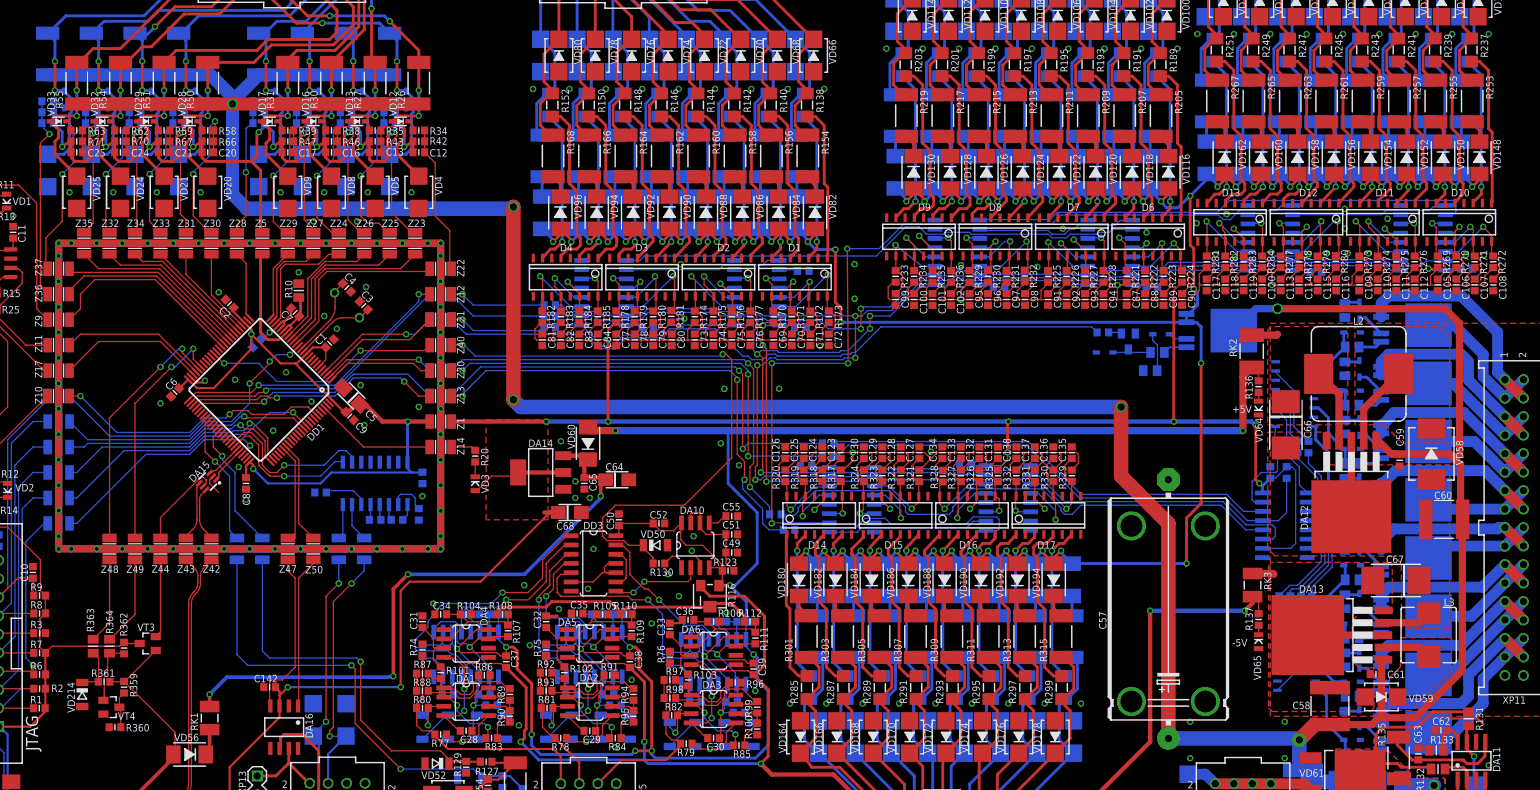
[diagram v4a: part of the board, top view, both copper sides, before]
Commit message: fixed reference poit for optocoupler
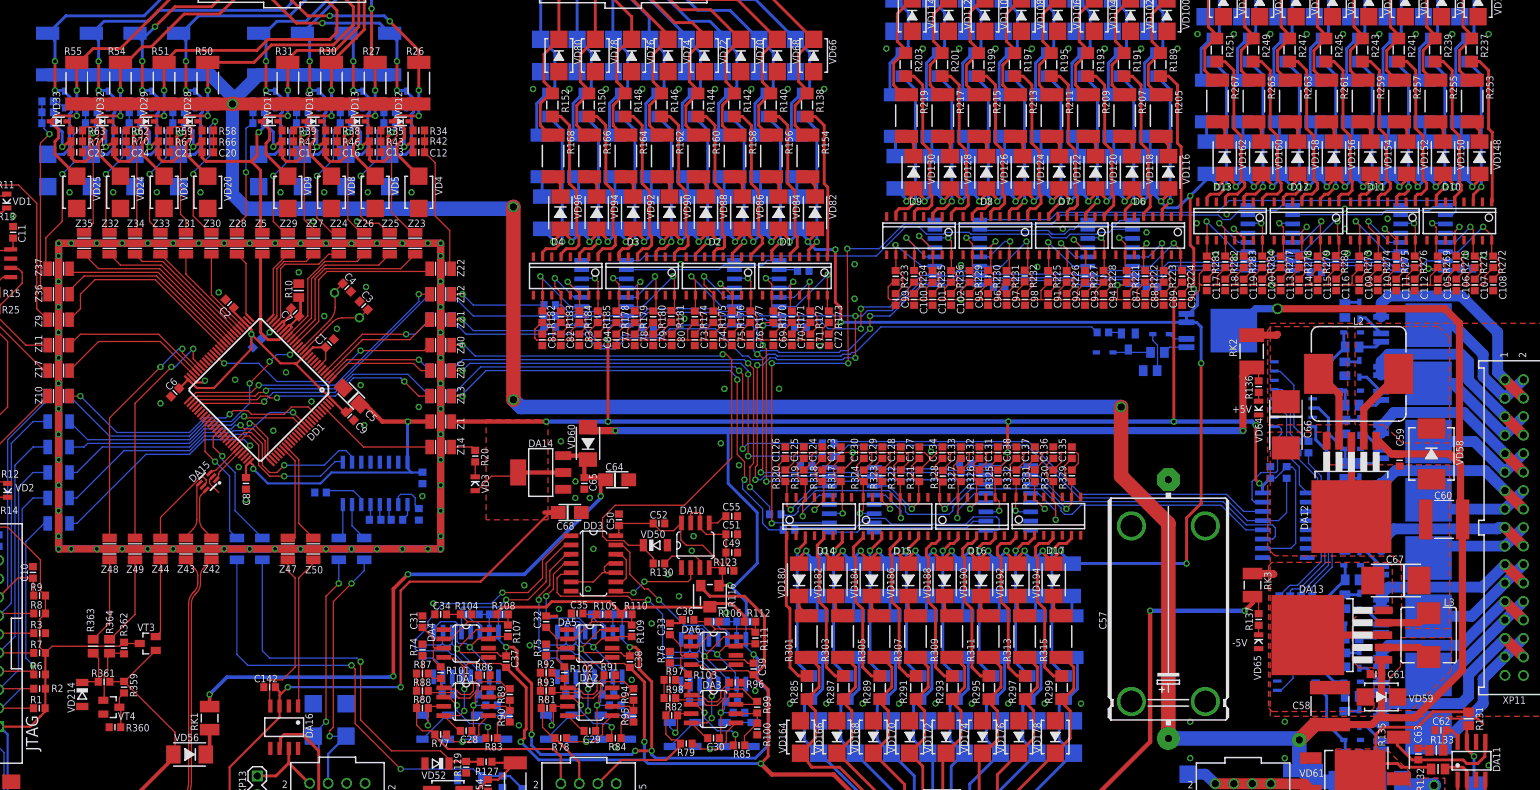
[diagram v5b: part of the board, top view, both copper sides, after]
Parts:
- moved D18 1.44 mm to (184.7, 74.2)
- moved D1 1.44 mm to (116.2, 90.5)
- moved D14 1.44 mm to (119.5, 57.5)
- moved D2 1.44 mm to (105.8, 90.5)
- moved D3 1.44 mm to (95.2, 90.5)
- moved D4 1.44 mm to (84.8, 90.5)
- moved D10 1.44 mm to (207.6, 98.0)
- moved D11 1.44 mm to (197.1, 98.0)
- moved D12 1.44 mm to (186.6, 98.0)
- moved D13 1.44 mm to (176.1, 98.0)
- moved D15 1.44 mm to (129.9, 57.5)
- moved D16 1.44 mm to (140.4, 57.5)
- moved D6 1.44 mm to (164.8, 96.0)
- moved D7 1.44 mm to (154.3, 96.0)
- moved D8 1.44 mm to (143.8, 96.0)
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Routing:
- net N$60: track 2.11 -> 3.08 mm
- net N$59: track 5.20 -> 5.75 mm

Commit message: nop
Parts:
- DD2: device rom:SO-08 -> rom:SO08
- XP13: value PLD_1X2 -> PLD_1X02; device connector:PLD_1X2 -> connector:PLD_1X02
- moved C57 1.27 mm to (167.5, 44.7)
